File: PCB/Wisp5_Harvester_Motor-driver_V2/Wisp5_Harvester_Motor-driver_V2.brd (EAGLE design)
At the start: 30 x 30 mm, 29 parts, among them M1 PINHEAD_PINHD-1X2-1.27MM, M2 PINHEAD_PINHD-1X2-1.27MM, U1 BQ25570

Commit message: Routing WIP
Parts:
- moved R6 3.55 mm to (8.65, 24.0)
- moved R4 3.34 mm to (6.46, 5.60)
- moved R3 3.09 mm to (6.46, 2.55)
- moved R2 2.49 mm to (8.65, 27.0)
- moved VIN/GND 0.98 mm to (26.1, 27.0), turned to 180 degrees
- moved L2 0.68 mm to (9.10, 16.5), turned to 270 degrees
- moved U1 0.63 mm to (15.0, 21.0)
- moved R9 0.57 mm to (3.56, 19.5)
- moved R8 0.57 mm to (3.56, 22.6)
- moved R10 0.54 mm to (3.58, 16.5), turned to 0 degrees
- moved R7 0.51 mm to (3.56, 25.8)
- moved M2 0.46 mm to (27.4, 6.79)
- moved M1 0.43 mm to (2.60, 6.78)
- moved C5 0.32 mm to (20.5, 24.0)
- moved R1 0.25 mm to (8.65, 20.9)
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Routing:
- net VHARV: track 0.00 -> 20.1 mm
- net VSTOR: track 0.00 -> 16.4 mm, vias 0 -> 2
- net N$1: track 0.00 -> 15.6 mm
- net N$2: track 0.00 -> 7.59 mm
- net N$4: track 0.00 -> 6.95 mm
- net N$12: track 0.00 -> 5.46 mm
- net N$9: track 0.00 -> 4.13 mm
- net N$18: track 0.00 -> 3.87 mm
- net N$10: track 0.00 -> 3.79 mm
- net SDA: track 0.00 -> 3.66 mm
- net SCL: track 0.00 -> 2.92 mm
- net GND: track 0.00 -> 0.55 mm

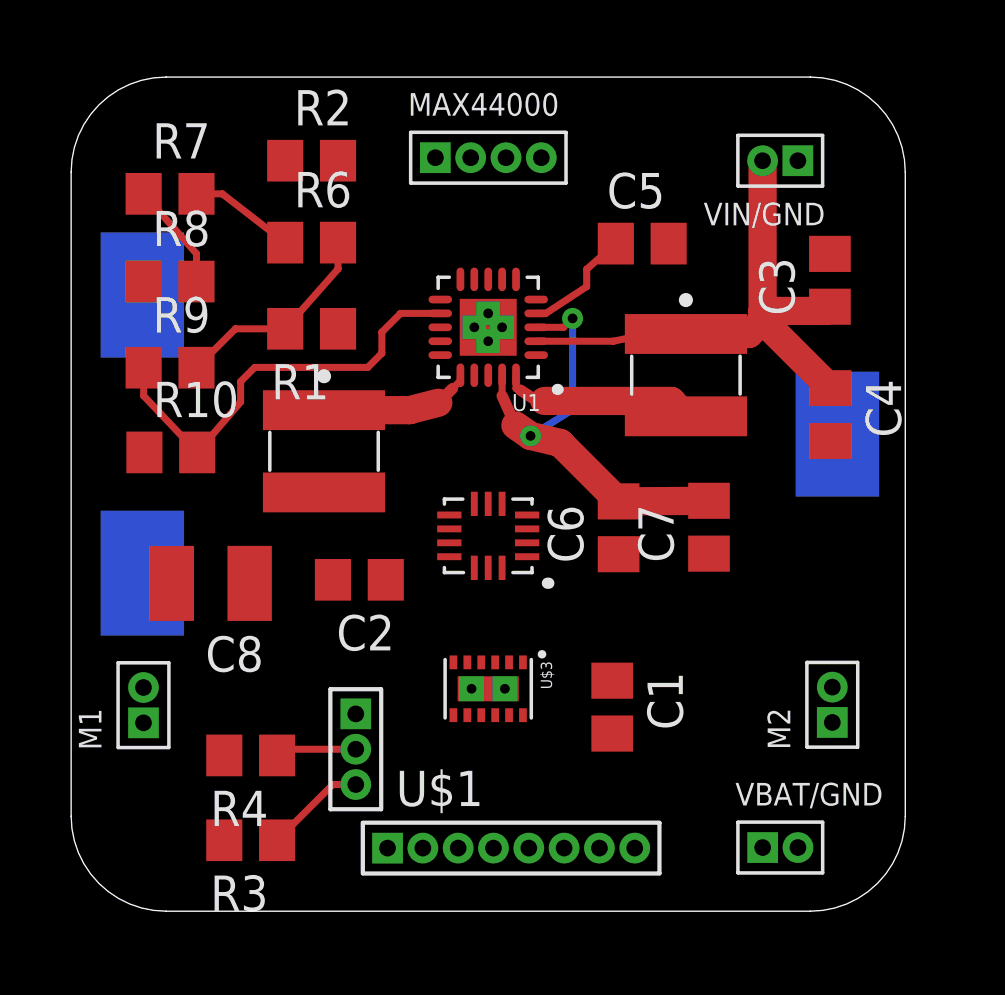
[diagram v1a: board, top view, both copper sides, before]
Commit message: Finished routing + fixed drv8836
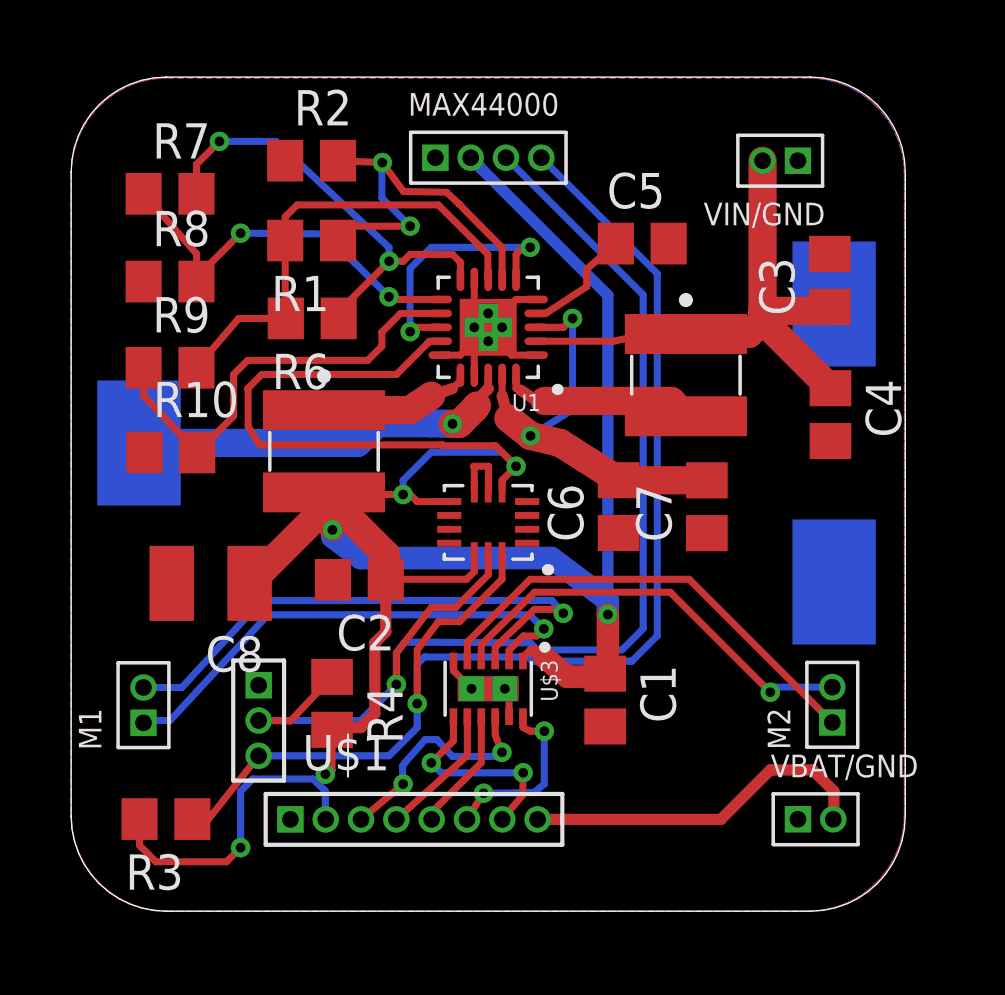
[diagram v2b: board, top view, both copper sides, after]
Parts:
- L1, L2: device robot_pcb2:LPS4018 -> Wisp5_Harvester_Motor-driver_V2:LPS4018
- U$1: device robot_pcb2:PINHEAD_WISP3X8-1.27MM -> Wisp5_Harvester_Motor-driver_V2:PINHEAD_WISP3X8-1.27MM
- U$3: device robot_pcb2:12WSON -> Wisp5_Harvester_Motor-driver_V2:12WSON
- moved U$1 8.45 mm to (5.47, 2.03)
- moved R4 3.47 mm to (9.38, 7.47), turned to 270 degrees
- moved R1 3.17 mm to (8.65, 24.1)
- moved R3 3.14 mm to (3.41, 3.31)
- moved R6 2.73 mm to (8.67, 21.3), turned to 180 degrees
- moved VBAT/GND 1.63 mm to (26.1, 3.31)
- moved C6 0.76 mm to (19.7, 14.6)
- moved C7 0.74 mm to (22.9, 14.5)
- moved U$2 0.48 mm to (15.0, 14.0)
- moved C1 0.36 mm to (19.2, 7.59)
- moved C9 0.34 mm to (14.9, 16.8), turned to 0 degrees
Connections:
- net GND: now also U$3.P$1, U$3.P$2
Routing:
- net VREG: track 0.00 -> 101.5 mm, vias 0 -> 6
- net SDA: track 3.66 -> 47.0 mm, vias 0 -> 1
- net SCL: track 2.92 -> 44.9 mm, vias 0 -> 1
- net AOUT2_M1: track 0.00 -> 20.2 mm, vias 0 -> 1
- net AOUT1_M1: track 0.00 -> 18.2 mm, vias 0 -> 1
- net BOUT2_M2: track 0.00 -> 16.9 mm
- net BOUT1_M2: track 0.00 -> 15.5 mm, vias 0 -> 1
- net GND: track 0.55 -> 14.9 mm
- net VBAT: track 0.00 -> 14.0 mm, vias 0 -> 1
- net N$13: track 0.00 -> 13.9 mm, vias 0 -> 2
- net N$10: track 3.79 -> 16.5 mm, vias 0 -> 2
- net VBOOST: track 0.00 -> 12.7 mm
- net N$18: track 3.87 -> 14.4 mm, vias 0 -> 2
- net N$2: track 7.59 -> 17.2 mm
- net VBAT_OK: track 0.00 -> 9.58 mm, vias 0 -> 2
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- added copper zone on layer 1, net GND
- added copper zone on layer 16, net GND
